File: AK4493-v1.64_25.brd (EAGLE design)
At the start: 89.9 x 64 mm, 138 parts, among them IC1 LT3042, IC2 AK4493, IC3 AK4493, IC4 LT3042, IC4A SN74ABT273DBR, IC5 LT3042, IC6 LT3042, IC7 LT3042, IC8 LT3042, J15 XR2A-0811-N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

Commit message: Updating board for breakout boards
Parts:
- added J21, J22: (no value), SparkFun-Connectors:1X10
- moved C18E 57.0 mm to (-20.8, 11.0)
- moved C19E 57.0 mm to (-17.8, 6.63)
- moved C20E 57.0 mm to (-7.97, 12.1)
- moved C21E 57.0 mm to (-11.5, 12.1)
- moved IC6 57.0 mm to (-13.0, 8.72)
- moved J18 57.0 mm to (-9.15, 4.91)
- moved R6E 57.0 mm to (-5.79, 5.33)
- moved R7E 57.0 mm to (-20.0, 7.18)
- moved R8E 57.0 mm to (-7.63, 8.95)
- moved C18F 43.8 mm to (-17.2, 30.3)
- moved C19F 43.8 mm to (-17.2, 25.9)
- moved C20F 43.8 mm to (-8.98, 33.4)
- moved C21F 43.8 mm to (-11.2, 31.4)
- moved IC8 43.8 mm to (-12.4, 28.0)
- moved J20 43.8 mm to (-8.59, 24.2)
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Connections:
- new net N$3: IC4A.10, J21.1
- new net N$4: IC4A.6, J21.5
- new net N$5: IC4A.16, J22.5
- net +3V3: now also J22.1
- net BCLK: now also J21.3, J22.3
- net DATA: now also J21.7, J22.7
- net DGND: now also J21.4, J22.4; no longer IC4A.10
- net LRCK: now also J21.8, J22.8
- net MCLK: now also J22.10
- net N$1: now also J21.10
- net N$23: now also J22.2
- net N$24: now also J22.6
- net N$25: now also J22.9
- net N$30: now also J21.2
- net N$31: now also J21.6
- net N$32: now also J21.9
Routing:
- net +3V3: track 178.7 -> 47.3 mm, vias 22 -> 0
- net VCC/2: track 52.3 -> 0.00 mm, vias 6 -> 3
- net +5V/1: track 95.7 -> 58.0 mm
- net +5V/4: track 20.7 -> 0.00 mm
- net N$25: track 20.9 -> 41.5 mm
- net +5V/5: track 81.9 -> 62.9 mm
- net SCL0: track 138.2 -> 124.2 mm, vias 3 -> 1
- net DIF0: track 78.2 -> 91.6 mm
- net SDA0: track 139.8 -> 127.3 mm, vias 3 -> 1
- net MCLK: track 84.7 -> 74.0 mm
- net N$30: track 20.6 -> 31.2 mm
- net N$3: track 0.00 -> 10.2 mm
- net PDN: track 130.5 -> 140.2 mm
- net VCC/1: track 9.64 -> 0.00 mm
- net VCC/3: track 9.64 -> 0.00 mm
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- removed copper zone on layer 16, net N$106
- removed copper zone on layer 16, net N$108
- removed copper zone on layer 16, net N$14
- removed copper zone on layer 16, net N$22
- removed copper zone on layer 16, net N$40
- removed copper zone on layer 16, net N$42
- removed copper zone on layer 16, net N$46
- removed copper zone on layer 16, net N$52
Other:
- board size 89.9 x 64 mm -> 123.4 x 88.4 mm

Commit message: Update
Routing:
- net PDN: track 140.2 -> 160.5 mm
- net MCLK: track 74.0 -> 94.0 mm
- net DATA: track 24.5 -> 42.9 mm, vias 2 -> 4
- net LRCK: track 33.9 -> 49.9 mm
- net N$30: track 31.2 -> 45.6 mm
- net N$32: track 22.5 -> 36.1 mm
- net BCLK: track 32.0 -> 44.5 mm
- net N$31: track 22.7 -> 34.7 mm
- net N$23: track 22.8 -> 31.8 mm
- net N$5: track 0.00 -> 4.46 mm
- net N$4: track 0.00 -> 4.46 mm
- net N$24: track 27.9 -> 32.4 mm
- net DIF0: track 91.6 -> 92.6 mm
- net DIF1: track 88.4 -> 89.3 mm
- net SDA0: track 127.3 -> 128.2 mm
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
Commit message: Progress
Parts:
- moved J18 115.3 mm to (74.0, 84.7), turned to 0 degrees
- moved IC6 110.1 mm to (70.2, 80.9), turned to 270 degrees
- moved IC5 92.8 mm to (10.1, 62.4)
- moved J17 92.8 mm to (13.9, 66.2)
- moved R7E 84.3 mm to (28.1, 76.4), turned to 90 degrees
- moved R8E 83.4 mm to (24.2, 86.0), turned to 180 degrees
- moved R6E 83.3 mm to (28.0, 81.5), turned to 90 degrees
- moved C19E 79.4 mm to (26.7, 72.4), turned to 0 degrees
- moved C20E 78.4 mm to (18.3, 86.0)
- moved C18E 75.1 mm to (14.6, 77.2), turned to 270 degrees
- moved C21E 74.9 mm to (14.6, 82.3), turned to 270 degrees
- moved J20 67.9 mm to (25.1, 83.1), turned to 0 degrees
- moved IC8 61.4 mm to (21.3, 79.3), turned to 270 degrees
- moved R7F 59.1 mm to (36.2, 46.5), turned to 90 degrees
- moved C19F 54.6 mm to (34.8, 42.5), turned to 0 degrees
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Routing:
- net PDN: track 160.5 -> 229.4 mm
- net N$31: track 34.7 -> 69.5 mm
- net N$32: track 36.1 -> 71.0 mm
- net N$30: track 45.6 -> 80.5 mm
- net SCL0: track 124.8 -> 159.0 mm
- net SDA0: track 128.2 -> 162.2 mm
- net N$24: track 32.4 -> 66.4 mm
- net DIF1: track 89.3 -> 123.3 mm
- net N$25: track 41.5 -> 75.5 mm
- net N$23: track 31.8 -> 65.9 mm
- net DIF0: track 92.6 -> 126.7 mm
- net MCLK: track 94.0 -> 124.6 mm
- net VCC/1: track 0.00 -> 22.1 mm
- net VCC/3: track 0.00 -> 22.0 mm
- net VCC/2: track 0.00 -> 22.0 mm, vias 3 -> 0
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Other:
- board size 123.4 x 88.4 mm -> 89.9 x 99.5 mm

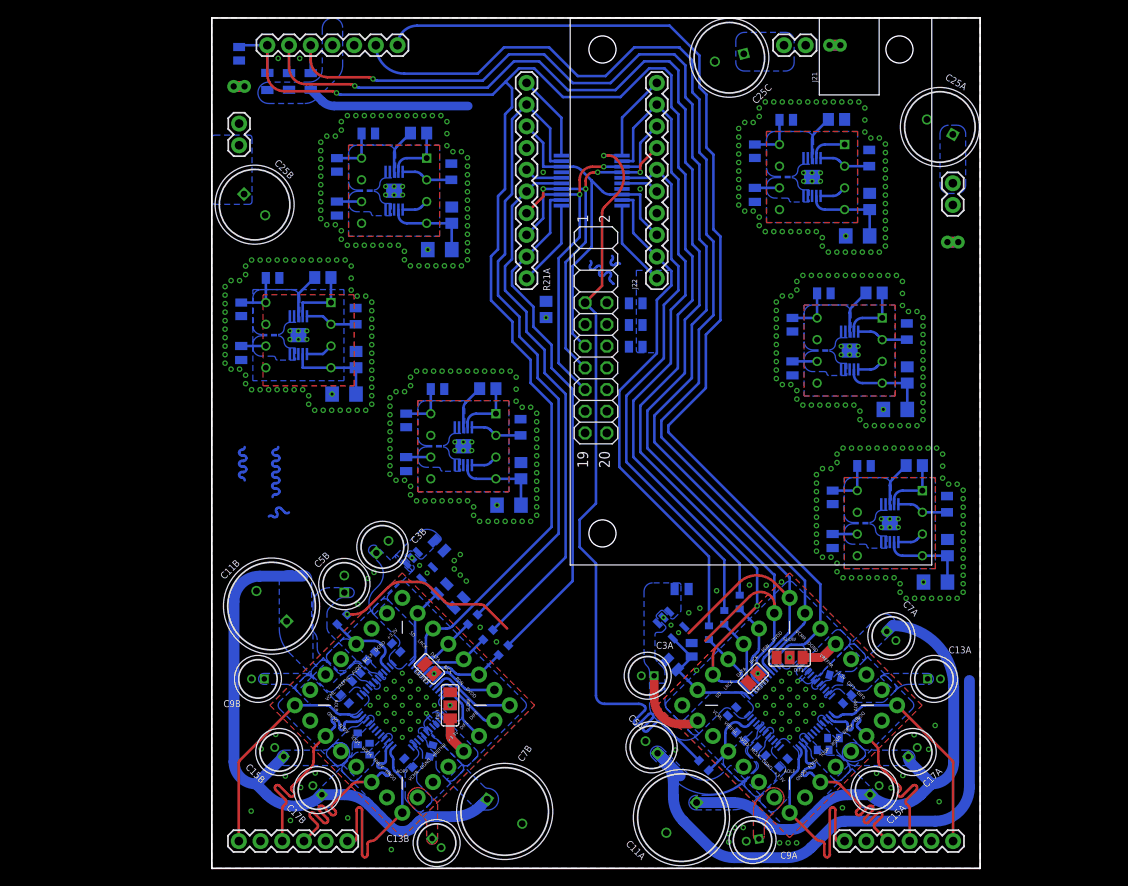
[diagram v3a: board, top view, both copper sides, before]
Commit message: Update Output stage with fusion export
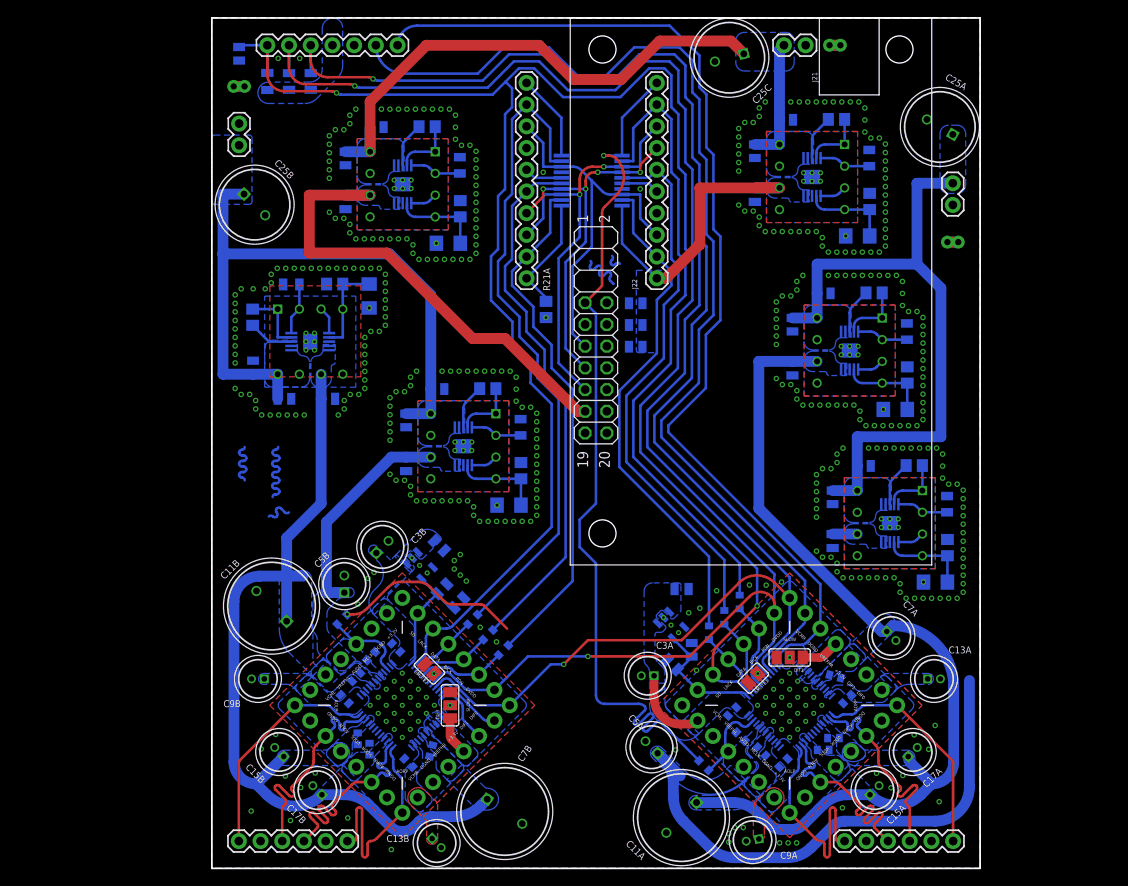
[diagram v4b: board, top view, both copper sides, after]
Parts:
- moved C19B 11.8 mm to (18.4, 67.0), turned to 270 degrees
- moved C21B 11.6 mm to (8.49, 54.9), turned to 180 degrees
- moved C18B 11.5 mm to (13.6, 54.9), turned to 180 degrees
- moved C20B 10.7 mm to (4.82, 58.6), turned to 90 degrees
- moved R8B 9.44 mm to (4.77, 64.5), turned to 90 degrees
- moved R7B 9.19 mm to (14.4, 68.4), turned to 0 degrees
- moved R6B 8.39 mm to (9.29, 68.3), turned to 0 degrees
- moved J17 6.28 mm to (7.70, 65.4), turned to 270 degrees
- moved IC5 1.58 mm to (11.5, 61.6), turned to 180 degrees
- moved C18E 1.25 mm to (15.6, 77.9)
- moved C19E 1.25 mm to (27.7, 73.1)
- moved C20E 1.25 mm to (19.3, 86.7)
- moved C21E 1.25 mm to (15.6, 83.1)
- moved IC8 1.25 mm to (22.3, 80.0)
- moved J20 1.25 mm to (26.1, 83.8)
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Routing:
- net VCC/2: track 22.0 -> 87.4 mm
- net VCC/1: track 22.1 -> 86.5 mm
- net VCC/3: track 22.0 -> 85.4 mm
- net +5V/3: track 2.88 -> 56.7 mm
- net +5V/1: track 60.9 -> 103.0 mm
- net +5V/2: track 69.2 -> 96.9 mm
- net SCL0: track 159.0 -> 185.9 mm, vias 1 -> 2
- net SDA0: track 162.2 -> 186.6 mm, vias 1 -> 2
- net +5V/4: track 2.88 -> 25.7 mm
- net N$1: track 10.2 -> 13.8 mm
- net +3V3: track 50.2 -> 53.7 mm
- net N$34: track 4.32 -> 7.25 mm
